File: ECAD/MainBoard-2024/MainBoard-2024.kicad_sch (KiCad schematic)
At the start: 65 parts, among them J1 XT60, J10 Conn_01x02, J11 Conn_01x03, J12 Conn_01x04, J13 Conn_01x03, J14 Conn_01x03, J16 XT30, J17 XT30, J18 Conn_01x02, J2 Conn_01x04, J20 BAU, J21 BAU, J22 Conn_01x04, J23 Conn_01x02, J26 BAU, J27 BAU, J28 Conn_01x02, J29 Conn_01x02, J3 ConStep1, J30 Conn_01x03, J4 Conn_01x02, J5 ConStep1, J6 ConStep1, J7 XT30, J8 Conn_01x02, J9 Conn_01x02, K2 FINDER-36.11, U1 Teensy3.5_All_Pins, U2 R-78B3.3-2.0, U3 R-78B12-2.0, U4 R-78B5.0-2.0

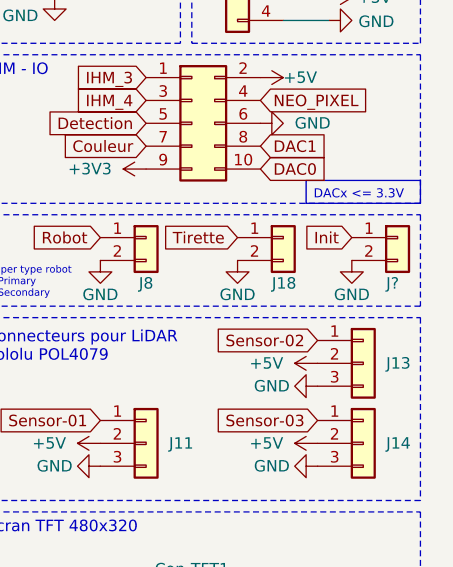
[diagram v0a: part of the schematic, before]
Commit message: Re-arrange schematic
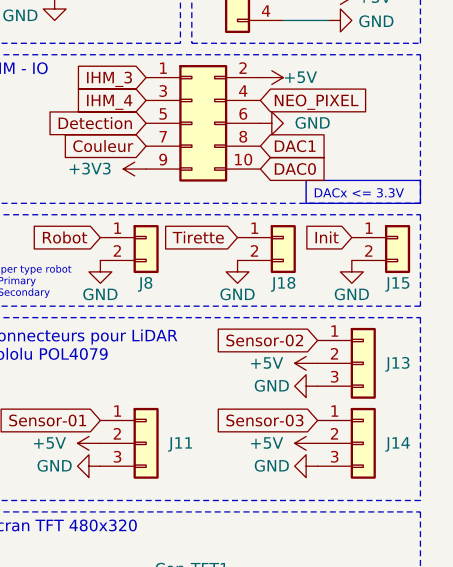
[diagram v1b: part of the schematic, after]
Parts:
- gave numbers to parts that had none: 1
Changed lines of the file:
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@@
   (symbol (lib_id "Connector_Generic:Conn_01x02") (at 279.4 109.22 0) (unit 1)
     (in_bom yes) (on_board yes) (dnp no)
-    (property "Reference" "J?" (at 278.13 114.3 0)
+    (property "Reference" "J15" (at 278.13 114.3 0)
       (effects (font (size 1.27 1.27)) (justify left))
     )
@@
       (project "MainBoard-2024"
         (path "/b1b0855c-c4b6-47dd-8ac8-2346963564b3"
-          (reference "J?") (unit 1)
+          (reference "J15") (unit 1)
         )
       )

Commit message: Clean positions
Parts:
- removed J16, J17: XT30, Connector_AMASS:AMASS_XT30U-F_1x02_P5.0mm_Vertical, symbol Connector_Generic:Conn_01x02
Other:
- moved on the sheet: J7
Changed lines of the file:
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@@
     (stroke (width 0) (type solid))
   )
-  (wire (pts (xy 196.85 152.4) (xy 196.85 160.02))
+  (wire (pts (xy 196.85 157.48) (xy 196.85 160.02))
     (stroke (width 0) (type default))
   )
@@
       (effects (font (size 1.27 1.27)) hide)
     )
-    (property "Value" "GND" (at 191.77 140.97 0)
+    (property "Value" "GND" (at 195.58 151.13 0)
       (effects (font (size 1.27 1.27)))
     )
@@
     )
   )
-  (symbol (lib_id "power:+24V") (at 196.85 152.4 0) (unit 1)
-    (in_bom yes) (on_board yes) (dnp no) (fields_autoplaced)
-    (property "Reference" "#PWR0157" (at 196.85 156.21 0)
+  (symbol (lib_id "power:+24V") (at 196.85 157.48 0) (unit 1)
+    (in_bom yes) (on_board yes) (dnp no)
+    (property "Reference" "#PWR0157" (at 196.85 161.29 0)
       (effects (font (size 1.27 1.27)) hide)
     )
-    (property "Value" "+24V" (at 196.85 147.32 0)
+    (property "Value" "+24V" (at 200.66 156.21 0)
       (effects (font (size 1.27 1.27)))
     )
-    (property "Footprint" "" (at 196.85 152.4 0)
+    (property "Footprint" "" (at 196.85 157.48 0)
       (effects (font (size 1.27 1.27)) hide)
     )
-    (property "Datasheet" "" (at 196.85 152.4 0)
+    (property "Datasheet" "" (at 196.85 157.48 0)
       (effects (font (size 1.27 1.27)) hide)
     )
@@
     )
   )
-  (symbol (lib_id "power:+24V") (at 218.44 140.97 90) (unit 1)
+  (symbol (lib_id "power:+24V") (at 213.36 148.59 90) (unit 1)
     (in_bom yes) (on_board yes) (dnp no) (fields_autoplaced)
-    (property "Reference" "#PWR0189" (at 222.25 140.97 0)
+    (property "Reference" "#PWR0189" (at 217.17 148.59 0)
       (effects (font (size 1.27 1.27)) hide)
     )
-    (property "Value" "+24V" (at 214.63 140.9699 90)
+    (property "Value" "+24V" (at 209.55 148.5899 90)
       (effects (font (size 1.27 1.27)) (justify left))
     )
-    (property "Footprint" "" (at 218.44 140.97 0)
+    (property "Footprint" "" (at 213.36 148.59 0)
       (effects (font (size 1.27 1.27)) hide)
     )
-    (property "Datasheet" "" (at 218.44 140.97 0)
+    (property "Datasheet" "" (at 213.36 148.59 0)
       (effects (font (size 1.27 1.27)) hide)
     )
@@
       (effects (font (size 1.27 1.27)) (justify right))
     )
-    (property "Value" "BAU" (at 189.9921 139.036 90)
+    (property "Value" "BAU" (at 190.5 140.97 90)
       (effects (font (size 1.27 1.27)) (justify right))
     )
@@
     )
   )
-  (symbol (lib_id "power:+24V") (at 218.44 158.75 90) (unit 1)
-    (in_bom yes) (on_board yes) (dnp no) (fields_autoplaced)
-    (property "Reference" "#PWR0185" (at 222.25 158.75 0)
-      (effects (font (size 1.27 1.27)) hide)
-    )
-    (property "Value" "+24V" (at 214.63 158.7499 90)
-      (effects (font (size 1.27 1.27)) (justify left))
-    )
-    (property "Footprint" "" (at 218.44 158.75 0)
-      (effects (font (size 1.27 1.27)) hide)
-    )
-    (property "Datasheet" "" (at 218.44 158.75 0)
-      (effects (font (size 1.27 1.27)) hide)
-    )
-    (pin "1")
-    (instances
-      (project "MainBoard-2024"
-        (path "/b1b0855c-c4b6-47dd-8ac8-2346963564b3"
-          (reference "#PWR0185") (unit 1)
-        )
-      )
-    )
-  )
   (symbol (lib_id "Regulator_Switching:R-78B5.0-2.0") (at 187.96 27.94 0) (unit 1)
     (in_bom yes) (on_board yes) (dnp no)
@@
     )
   )
-  (symbol (lib_id "power:GND") (at 218.44 161.29 270) (unit 1)
-    (in_bom yes) (on_board yes) (dnp no)
-    (property "Reference" "#PWR0187" (at 212.09 161.29 0)
-      (effects (font (size 1.27 1.27)) hide)
-    )
-    (property "Value" "GND" (at 213.36 161.29 90)
-      (effects (font (size 1.27 1.27)))
-    )
-    (property "Footprint" "" (at 218.44 161.29 0)
-      (effects (font (size 1.27 1.27)) hide)
-    )
-    (property "Datasheet" "" (at 218.44 161.29 0)
-      (effects (font (size 1.27 1.27)) hide)
-    )
-    (pin "1")
-    (instances
-      (project "MainBoard-2024"
-        (path "/b1b0855c-c4b6-47dd-8ac8-2346963564b3"
-          (reference "#PWR0187") (unit 1)
-        )
-      )
-    )
-  )
   (symbol (lib_id "power:+3V3") (at 262.89 148.59 270) (unit 1)
     (in_bom yes) (on_board yes) (dnp no) (fields_autoplaced)
@@
     )
   )
-  (symbol (lib_id "Connector_Generic:Conn_01x02") (at 223.52 161.29 0) (mirror x) (unit 1)
-    (in_bom yes) (on_board yes) (dnp no)
-    (property "Reference" "J17" (at 223.52 163.83 0)
-      (effects (font (size 1.27 1.27)))
-    )
-    (property "Value" "XT30" (at 227.33 160.02 0)
-      (effects (font (size 1.27 1.27)))
-    )
-    (property "Footprint" "Connector_AMASS:AMASS_XT30U-F_1x02_P5.0mm_Vertical" (at 223.52 161.29 0)
-      (effects (font (size 1.27 1.27)) hide)
-    )
-    (property "Datasheet" "~" (at 223.52 161.29 0)
-      (effects (font (size 1.27 1.27)) hide)
-    )
-    (pin "1")
-    (pin "2")
-    (instances
-      (project "MainBoard-2024"
-        (path "/b1b0855c-c4b6-47dd-8ac8-2346963564b3"
-          (reference "J17") (unit 1)
-        )
-      )
-    )
-  )
   (symbol (lib_id "Connector_Generic:Conn_01x04") (at 234.95 76.2 0) (mirror y) (unit 1)
     (in_bom yes) (on_board yes) (dnp no)
@@
     )
   )
-  (symbol (lib_id "power:GND") (at 218.44 152.4 270) (unit 1)
-    (in_bom yes) (on_board yes) (dnp no)
-    (property "Reference" "#PWR0186" (at 212.09 152.4 0)
-      (effects (font (size 1.27 1.27)) hide)
-    )
-    (property "Value" "GND" (at 213.36 152.4 90)
-      (effects (font (size 1.27 1.27)))
-    )
-    (property "Footprint" "" (at 218.44 152.4 0)
-      (effects (font (size 1.27 1.27)) hide)
-    )
-    (property "Datasheet" "" (at 218.44 152.4 0)
-      (effects (font (size 1.27 1.27)) hide)
-    )
-    (pin "1")
-    (instances
-      (project "MainBoard-2024"
-        (path "/b1b0855c-c4b6-47dd-8ac8-2346963564b3"
-          (reference "#PWR0186") (unit 1)
-        )
-      )
-    )
-  )
   (symbol (lib_id "Connector_Generic:Conn_01x02") (at 208.28 115.57 0) (unit 1)
     (in_bom yes) (on_board yes) (dnp no)
@@
     )
   )
-  (symbol (lib_id "power:+24V") (at 218.44 149.86 90) (unit 1)
-    (in_bom yes) (on_board yes) (dnp no) (fields_autoplaced)
-    (property "Reference" "#PWR0158" (at 222.25 149.86 0)
-      (effects (font (size 1.27 1.27)) hide)
-    )
-    (property "Value" "+24V" (at 214.63 149.8599 90)
-      (effects (font (size 1.27 1.27)) (justify left))
-    )
-    (property "Footprint" "" (at 218.44 149.86 0)
-      (effects (font (size 1.27 1.27)) hide)
-    )
-    (property "Datasheet" "" (at 218.44 149.86 0)
-      (effects (font (size 1.27 1.27)) hide)
-    )
-    (pin "1")
-    (instances
-      (project "MainBoard-2024"
-        (path "/b1b0855c-c4b6-47dd-8ac8-2346963564b3"
-          (reference "#PWR0158") (unit 1)
-        )
-      )
-    )
-  )
   (symbol (lib_id "power:GND") (at 46.99 45.72 270) (unit 1)
     (in_bom yes) (on_board yes) (dnp no) (fields_autoplaced)
@@
     )
   )
-  (symbol (lib_id "Connector_Generic:Conn_01x02") (at 223.52 143.51 0) (mirror x) (unit 1)
+  (symbol (lib_id "Connector_Generic:Conn_01x02") (at 218.44 151.13 0) (mirror x) (unit 1)
     (in_bom yes) (on_board yes) (dnp no)
-    (property "Reference" "J7" (at 223.52 146.05 0)
+    (property "Reference" "J7" (at 218.44 153.67 0)
       (effects (font (size 1.27 1.27)))
     )
-    (property "Value" "XT30" (at 227.33 142.24 0)
+    (property "Value" "XT30" (at 222.25 149.86 0)
       (effects (font (size 1.27 1.27)))
     )
-    (property "Footprint" "Connector_AMASS:AMASS_XT30U-F_1x02_P5.0mm_Vertical" (at 223.52 143.51 0)
+    (property "Footprint" "Connector_AMASS:AMASS_XT30U-F_1x02_P5.0mm_Vertical" (at 218.44 151.13 0)
       (effects (font (size 1.27 1.27)) hide)
     )
-    (property "Datasheet" "~" (at 223.52 143.51 0)
+    (property "Datasheet" "~" (at 218.44 151.13 0)
       (effects (font (size 1.27 1.27)) hide)
     )
@@
     )
   )
-  (symbol (lib_id "power:GND") (at 218.44 143.51 270) (unit 1)
+  (symbol (lib_id "power:GND") (at 213.36 151.13 270) (unit 1)
     (in_bom yes) (on_board yes) (dnp no)
-    (property "Reference" "#PWR0188" (at 212.09 143.51 0)
+    (property "Reference" "#PWR0188" (at 207.01 151.13 0)
       (effects (font (size 1.27 1.27)) hide)
     )
-    (property "Value" "GND" (at 213.36 143.51 90)
+    (property "Value" "GND" (at 208.28 151.13 90)
       (effects (font (size 1.27 1.27)))
     )
-    (property "Footprint" "" (at 218.44 143.51 0)
+    (property "Footprint" "" (at 213.36 151.13 0)
       (effects (font (size 1.27 1.27)) hide)
     )
-    (property "Datasheet" "" (at 218.44 143.51 0)
+    (property "Datasheet" "" (at 213.36 151.13 0)
       (effects (font (size 1.27 1.27)) hide)
     )
@@
         )
       )
-    )
-  )
-  (symbol (lib_id "Connector_Generic:Conn_01x02") (at 223.52 152.4 0) (mirror x) (unit 1)
-    (in_bom yes) (on_board yes) (dnp no)
-    (property "Reference" "J16" (at 223.52 154.94 0)
-      (effects (font (size 1.27 1.27)))
-    )
-    (property "Value" "XT30" (at 227.33 151.13 0)
-      (effects (font (size 1.27 1.27)))
-    )
-    (property "Footprint" "Connector_AMASS:AMASS_XT30U-F_1x02_P5.0mm_Vertical" (at 223.52 152.4 0)
-      (effects (font (size 1.27 1.27)) hide)
-    )
-    (property "Datasheet" "~" (at 223.52 152.4 0)
-      (effects (font (size 1.27 1.27)) hide)
-    )
-    (pin "1")
-    (pin "2")
-    (instances
-      (project "MainBoard-2024"
-        (path "/b1b0855c-c4b6-47dd-8ac8-2346963564b3"
-          (reference "J16") (unit 1)
-        )
-      )

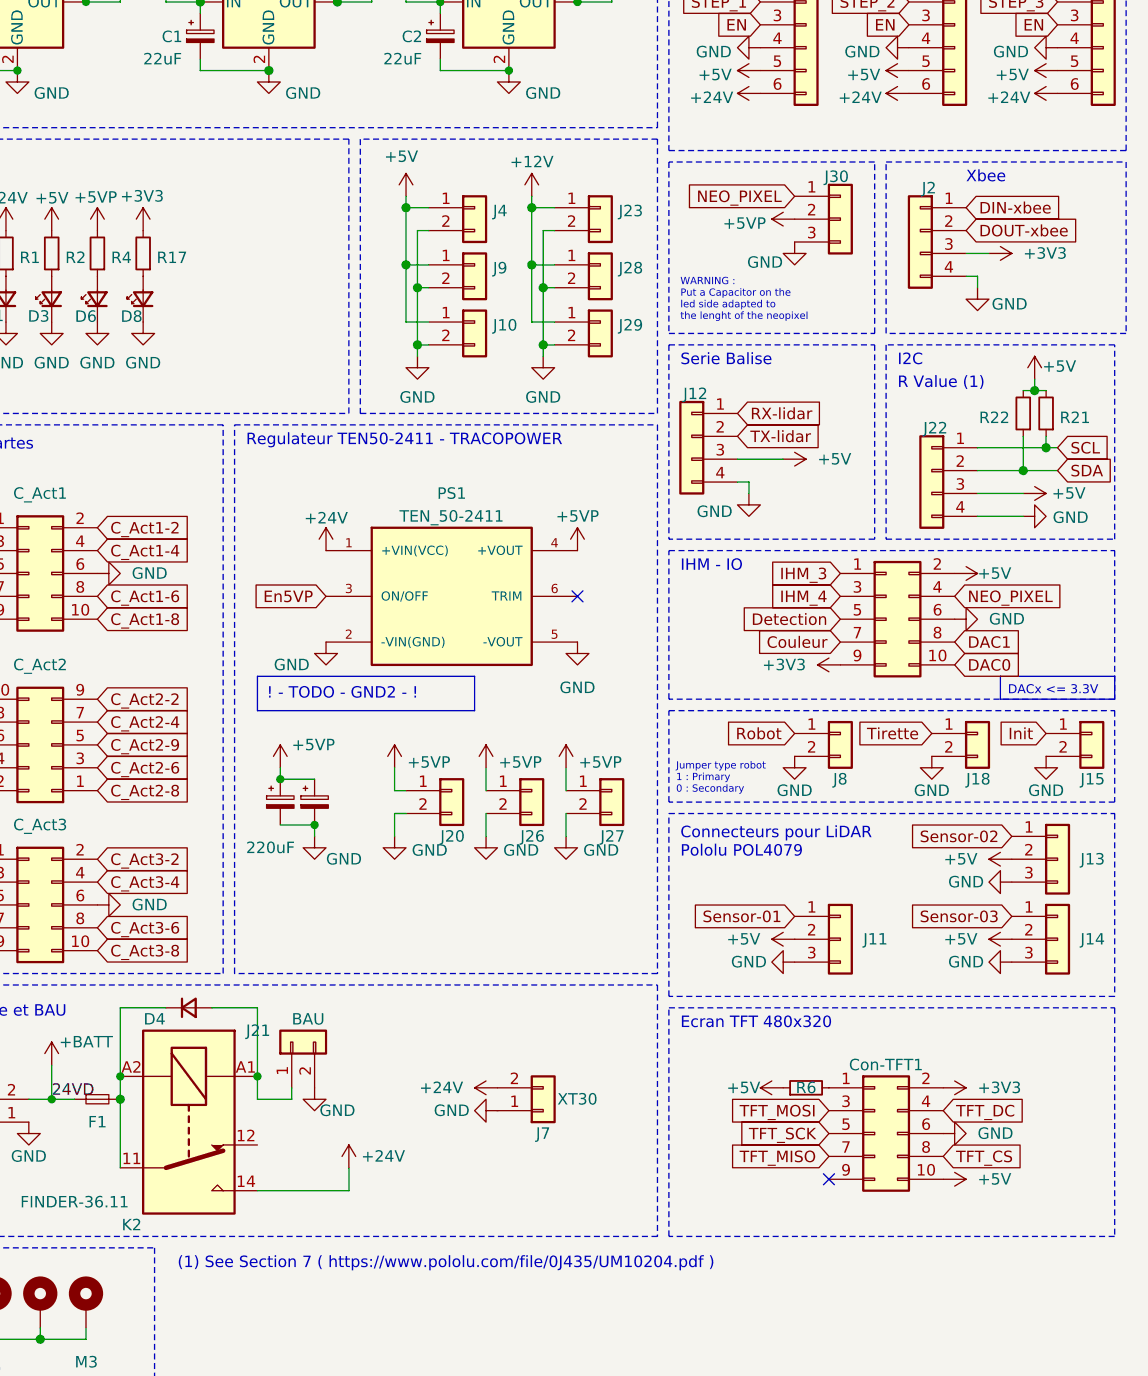
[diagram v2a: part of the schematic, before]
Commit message: First test trace
PCB Trace with poor optimisation and bad width to check the board before final trace.
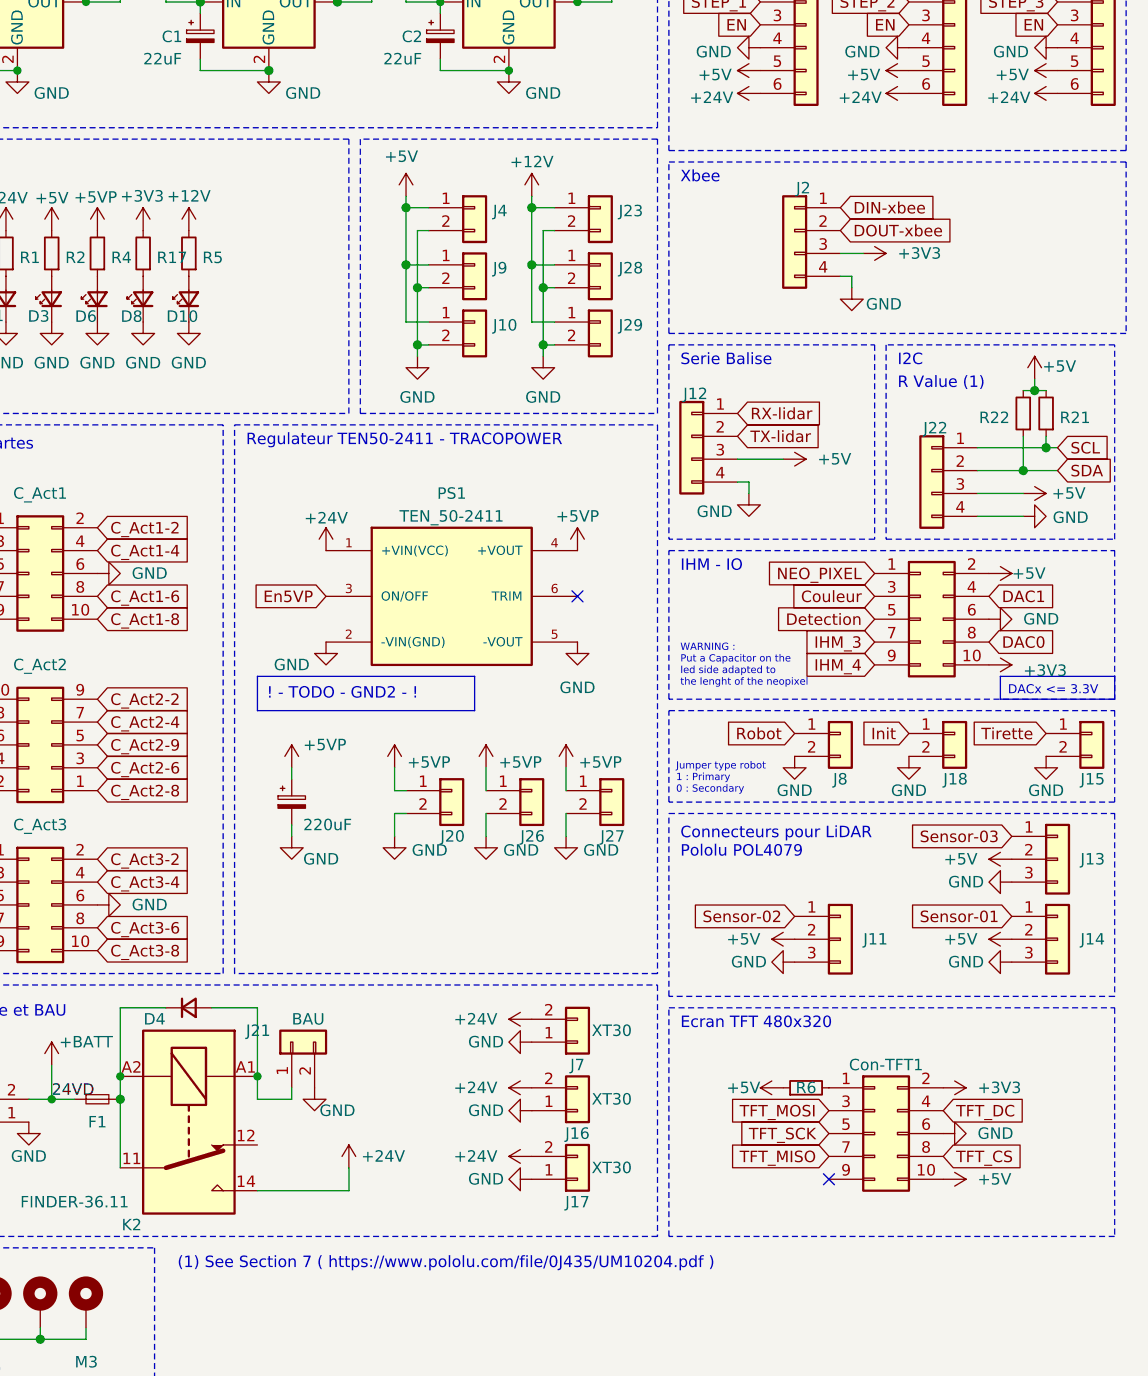
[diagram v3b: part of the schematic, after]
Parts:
- removed C4: 220uF, Capacitor_THT:CP_Radial_D8.0mm_P3.80mm, symbol Device:CP_Small
- removed J30: Conn_01x03, Connector_Molex:Molex_KK-254_AE-6410-03A_1x03_P2.54mm_Vertical, symbol Connector_Generic:Conn_01x03
- added D10: LED_Small, LED_SMD:LED_1206_3216Metric_Pad1.42x1.75mm_HandSolder, symbol Device:LED_Small
- added J16, J17: XT30, Connector_AMASS:AMASS_XT30U-F_1x02_P5.0mm_Vertical, symbol Connector_Generic:Conn_01x02
- added R5: R_Small, Resistor_SMD:R_1206_3216Metric_Pad1.30x1.75mm_HandSolder, symbol Device:R_Small
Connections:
- net +12V: now also R5.2
- net +24V: now also J16.2 (Pin_2), J17.2 (Pin_2)
- net +3V3: now also IHM-IO1.10 (Pin_10); no longer IHM-IO1.9 (Pin_9)
- net Couleur: now also IHM-IO1.3 (Pin_3); no longer IHM-IO1.7 (Pin_7)
- net DAC0: now also IHM-IO1.8 (Pin_8); no longer IHM-IO1.10 (Pin_10)
- net DAC1: now also IHM-IO1.4 (Pin_4); no longer IHM-IO1.8 (Pin_8)
- net GND: now also D10.1 (K), J16.1 (Pin_1), J17.1 (Pin_1)
- net IHM_3: now also IHM-IO1.7 (Pin_7); no longer IHM-IO1.1 (Pin_1)
- net IHM_4: now also IHM-IO1.9 (Pin_9); no longer IHM-IO1.3 (Pin_3)
- net Init: now also J18.1 (Pin_1); no longer J15.1 (Pin_1)
- net NEO_PIXEL: now also IHM-IO1.1 (Pin_1); no longer IHM-IO1.4 (Pin_4)
- net Sensor-01: now also J14.1 (Pin_1); no longer J11.1 (Pin_1)
- net Sensor-02: now also J11.1 (Pin_1); no longer J13.1 (Pin_1)
- net Sensor-03: now also J13.1 (Pin_1); no longer J14.1 (Pin_1)
- net Tirette: now also J15.1 (Pin_1); no longer J18.1 (Pin_1)
- new net: D10.2 (A), R5.1
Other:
- moved on the sheet: J18, J2, J7
